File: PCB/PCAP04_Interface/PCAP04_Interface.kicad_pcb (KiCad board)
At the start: 2 copper layers, 80.3 x 118.4 mm, 56 parts, among them IC1 PCAP04-AQFM-24, IC2 PCAP04-AQFM-24, IC3 PCAP04-AQFM-24, J1 Conn_01x04, J2 43045-2022, J3 MEM2067-02-180-00-A, U1 PCAP_04-eva-board, U2 ESP-WROOM-32-DEVBOARD

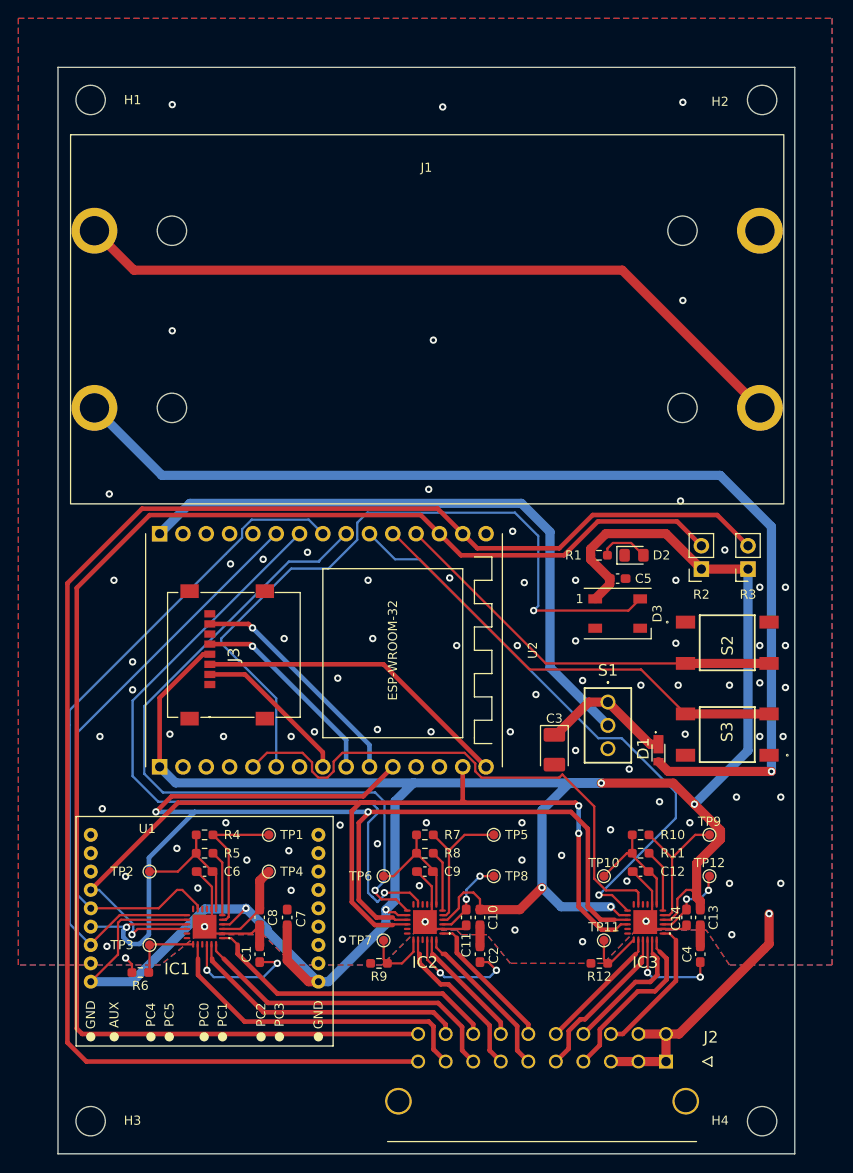
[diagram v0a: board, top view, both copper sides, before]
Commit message: Edited PCB so battery is on the back
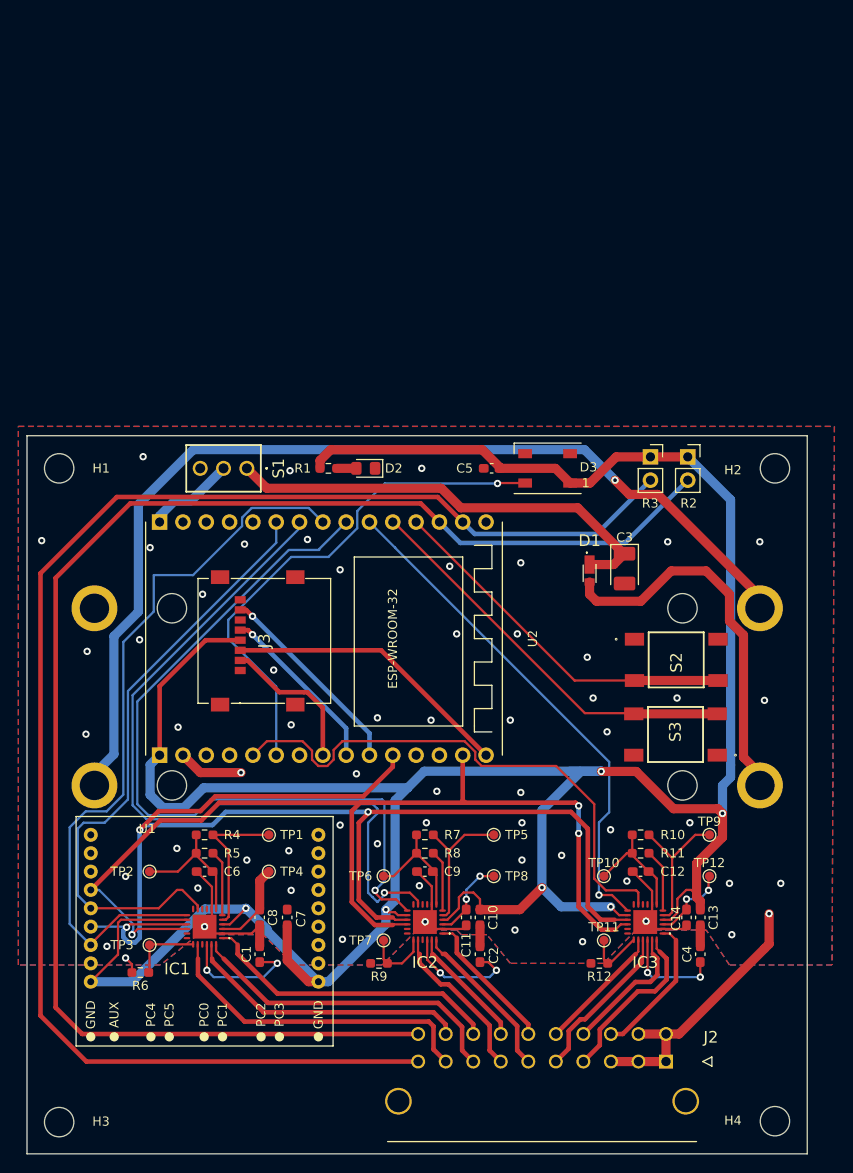
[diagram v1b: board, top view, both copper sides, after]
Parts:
- J1: moved to B.Cu
- moved S1 46.9 mm to (124.0, 73.7), turned to 90 degrees
- moved J1 41.1 mm to (143.6, 98.6), turned to 180 degrees
- moved H1 40.3 mm to (103.5, 73.7)
- moved H2 40.2 mm to (181.5, 73.7)
- moved R1 31.0 mm to (132.8, 73.7)
- moved D2 30.7 mm to (136.9, 73.7), turned to 180 degrees
- moved C3 21.2 mm to (165.1, 84.6)
- moved D1 21.0 mm to (161.3, 85.1)
- moved C5 18.2 mm to (150.6, 73.7), turned to 180 degrees
- moved D3 17.6 mm to (156.7, 73.7), turned to 180 degrees
- moved R3 16.2 mm to (167.9, 72.4), turned to 0 degrees
- moved R2 12.3 mm to (172.0, 72.4), turned to 0 degrees
- moved S2 5.87 mm to (170.7, 94.5)
- moved S3 5.64 mm to (170.7, 102.7)
- moved J3 3.65 mm to (121.0, 92.5)
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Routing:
- net Net-(D1-Pad2): track 118.5 -> 40.2 mm, vias 1 -> 0
- net +6V: track 68.9 -> 9.77 mm
- net +3V3: track 280.5 -> 325.1 mm
- net +BATT: track 14.3 -> 49.3 mm
- net Net-(J1-Pad2): track 80.5 -> 108.1 mm, vias 0 -> 1
- net LED_DATA: track 79.3 -> 56.5 mm
- net PCAP3_EN: track 63.5 -> 55.7 mm
- net GND: track 75.8 -> 82.9 mm, vias 86 -> 61
- net PR2-SENSE: track 171.3 -> 165.4 mm
- net PCAP2_EN: track 79.3 -> 85.0 mm
- net BUTTON2: track 49.1 -> 44.0 mm
- net PCAP1_EN: track 75.8 -> 80.9 mm
- net PCAP2_INT: track 78.8 -> 83.3 mm
- net BUTTON1: track 44.3 -> 40.0 mm
- net Net-(D2-Pad2): track 5.47 -> 2.13 mm
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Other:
- board size 80.3 x 118.4 mm -> 85 x 78.2 mm

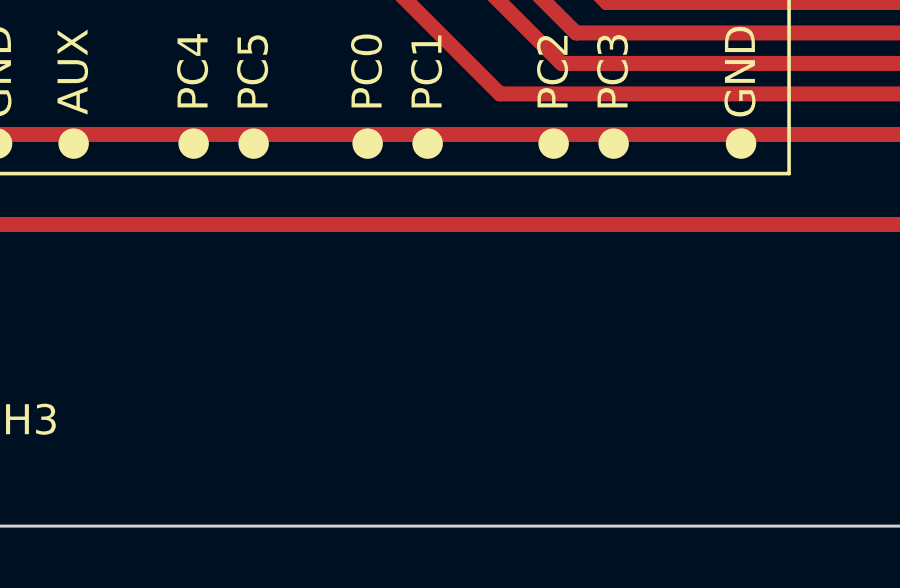
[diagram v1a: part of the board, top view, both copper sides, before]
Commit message: Added logos and text on PCB
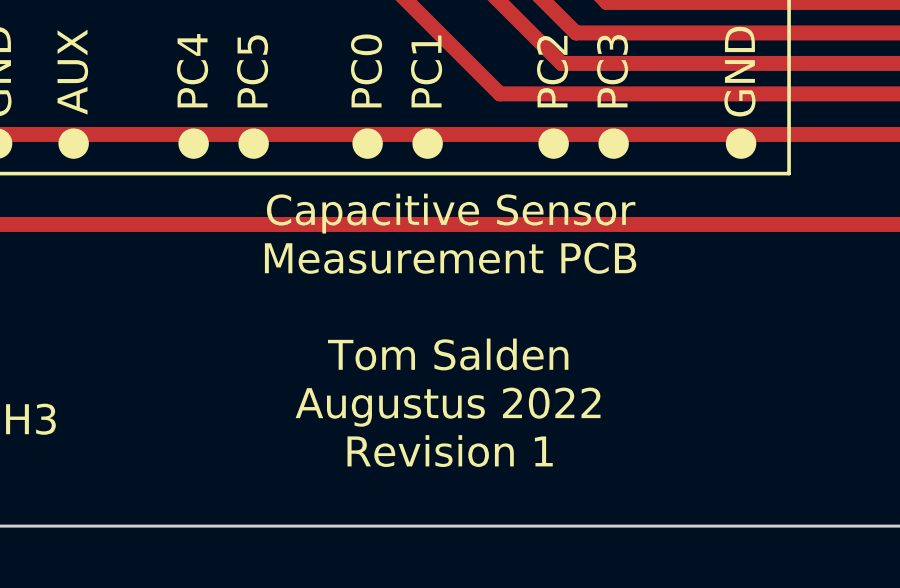
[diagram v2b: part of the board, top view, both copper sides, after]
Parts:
- added G***: LOGO, FootrpintLib:ECSEL_LOGO, B.Cu at (119.9, 124.6)
- added G***: LOGO, FootrpintLib:TUD_logo, B.Cu at (159.1, 124.2)
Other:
- board text added: "Capacitive Sensor Measurement PCB Tom Salden Augustus 2022 Revision 1"
- board text added: "Capacitive Sensor Readout Board Based on PCAP04 CDC's Using ESP32-WROOM for processing Used for MEMS Capacitive Pressure Sensors"

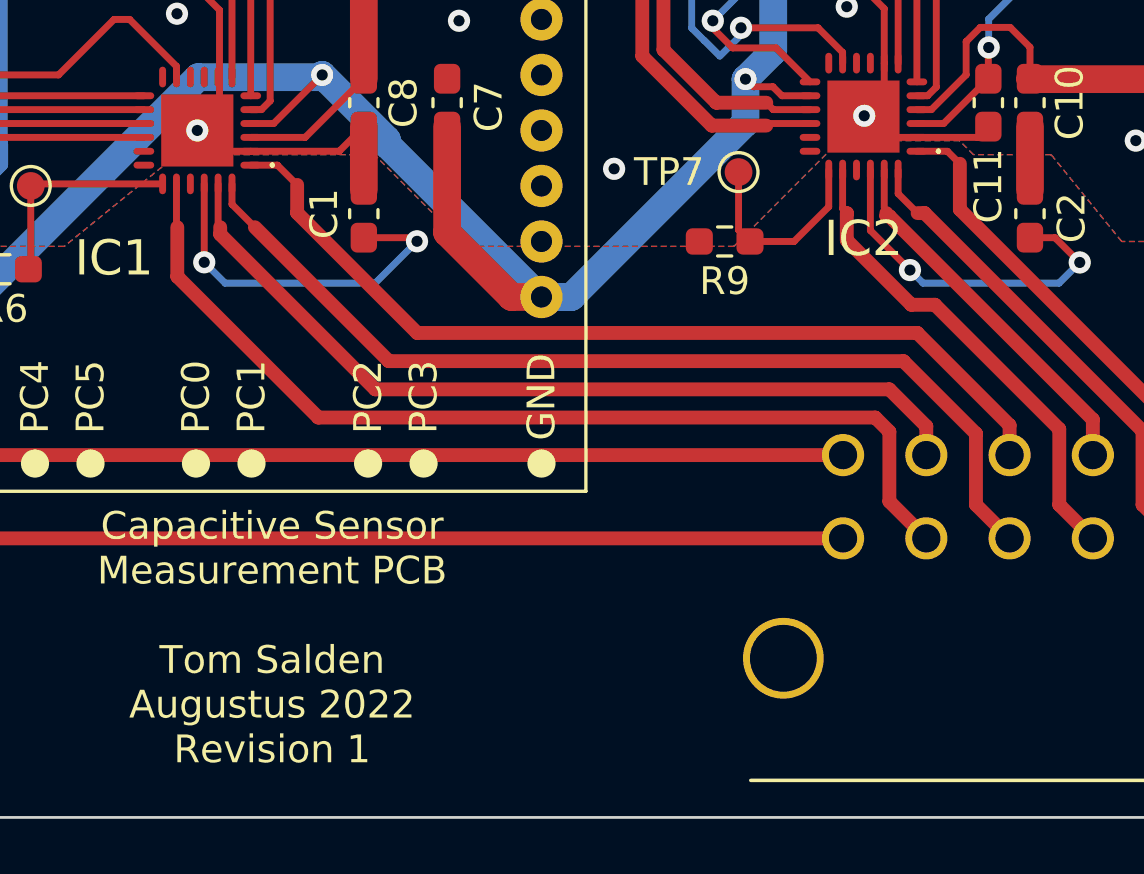
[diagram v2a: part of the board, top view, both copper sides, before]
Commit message: Added breakout for C1.5 and C2.5
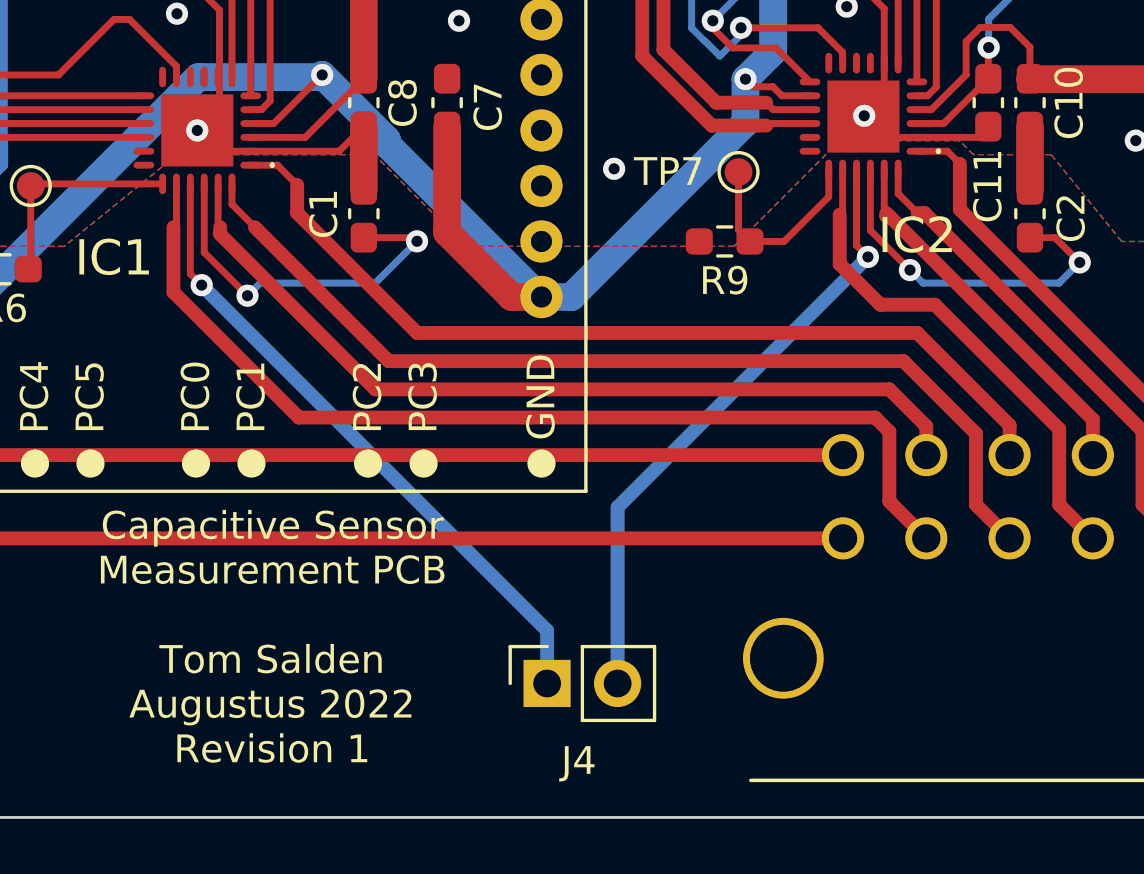
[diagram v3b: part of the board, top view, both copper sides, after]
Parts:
- removed the G*** at (159.1, 124.2)
- added J4: Conn_01x02, Connector_PinSocket_2.54mm:PinSocket_1x02_P2.54mm_Vertical, F.Cu at (132.0, 143.5)
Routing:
- net C1.5: track 0.00 -> 23.3 mm, vias 0 -> 1
- net C2.5: track 0.00 -> 22.4 mm, vias 0 -> 1
- net C2.4: track 17.5 -> 18.2 mm
- net C1.4: track 35.7 -> 36.2 mm
